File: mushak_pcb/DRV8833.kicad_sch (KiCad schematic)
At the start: 7 parts, among them M1 motor, M2 motor, U3 DRV8833PW

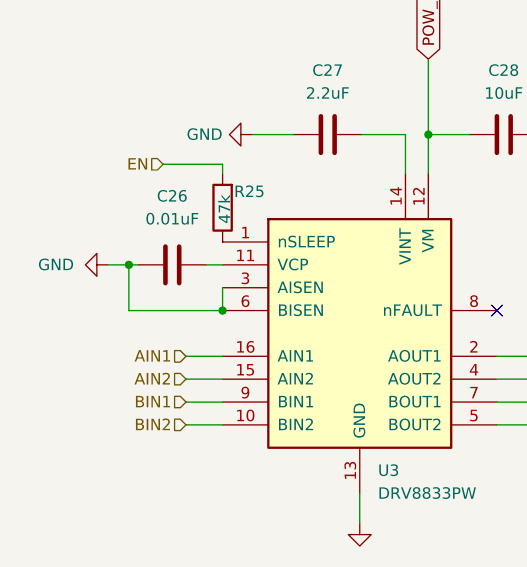
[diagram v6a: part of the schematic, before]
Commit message: corrected encoder and motor driver schematics
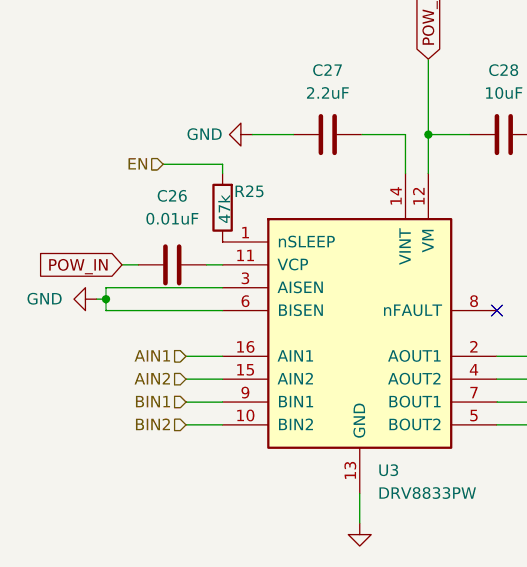
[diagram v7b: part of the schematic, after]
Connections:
- net GND: no longer C26.1
- net POW_IN: now also C26.1
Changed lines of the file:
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@@
     (comment 1 "Designed by - Chinmay Lonkar")
-  )
-  (junction (at 132.08 95.25) (diameter 0) (color 0 0 0 0)
   )
   (junction (at 154.94 75.692) (diameter 0) (color 0 0 0 0)
   )
-  (junction (at 121.666 90.17) (diameter 0) (color 0 0 0 0)
+  (junction (at 119.126 93.98) (diameter 0) (color 0 0 0 0)
   )
   (no_connect (at 162.56 95.25))
@@
     (stroke (width 0) (type default) (color 0 0 0 0))
   )
-  (wire (pts (xy 121.666 90.17) (xy 122.682 90.17))
-    (stroke (width 0) (type default) (color 0 0 0 0))
-  )
   (wire (pts (xy 162.56 107.95) (xy 202.438 107.95))
     (stroke (width 0) (type default) (color 0 0 0 0))
   )
-  (wire (pts (xy 119.38 90.17) (xy 121.666 90.17))
+  (wire (pts (xy 120.904 90.17) (xy 122.682 90.17))
     (stroke (width 0) (type default) (color 0 0 0 0))
   )
@@
     (stroke (width 0) (type default) (color 0 0 0 0))
   )
+  (wire (pts (xy 119.126 95.25) (xy 132.08 95.25))
+    (stroke (width 0) (type default) (color 0 0 0 0))
+  )
   (wire (pts (xy 154.94 75.692) (xy 159.512 75.692))
     (stroke (width 0) (type default) (color 0 0 0 0))
   )
   (wire (pts (xy 147.32 115.57) (xy 147.32 118.872))
+    (stroke (width 0) (type default) (color 0 0 0 0))
+  )
+  (wire (pts (xy 132.08 92.71) (xy 119.126 92.71))
     (stroke (width 0) (type default) (color 0 0 0 0))
   )
@@
     (stroke (width 0) (type default) (color 0 0 0 0))
   )
-  (wire (pts (xy 121.666 95.25) (xy 121.666 90.17))
-    (stroke (width 0) (type default) (color 0 0 0 0))
-  )
   (wire (pts (xy 128.016 100.33) (xy 132.08 100.33))
     (stroke (width 0) (type default) (color 0 0 0 0))
   )
   (wire (pts (xy 125.476 78.994) (xy 132.08 78.994))
+    (stroke (width 0) (type default) (color 0 0 0 0))
+  )
+  (wire (pts (xy 118.11 93.98) (xy 119.126 93.98))
     (stroke (width 0) (type default) (color 0 0 0 0))
   )
@@
     (stroke (width 0) (type default) (color 0 0 0 0))
   )
-  (wire (pts (xy 162.56 102.87) (xy 222.25 102.87))
+  (wire (pts (xy 119.126 93.98) (xy 119.126 95.25))
     (stroke (width 0) (type default) (color 0 0 0 0))
   )
-  (wire (pts (xy 132.08 92.71) (xy 132.08 95.25))
+  (wire (pts (xy 162.56 102.87) (xy 222.25 102.87))
     (stroke (width 0) (type default) (color 0 0 0 0))
   )
@@
     (stroke (width 0) (type default) (color 0 0 0 0))
   )
-  (wire (pts (xy 132.08 95.25) (xy 121.666 95.25))
+  (wire (pts (xy 119.126 92.71) (xy 119.126 93.98))
     (stroke (width 0) (type default) (color 0 0 0 0))
   )
   (wire (pts (xy 130.302 90.17) (xy 132.08 90.17))
     (stroke (width 0) (type default) (color 0 0 0 0))
+  )
+  (global_label "POW_IN" (shape input) (at 120.904 90.17 180) (fields_autoplaced)
+    (effects (font (size 1.27 1.27)) (justify right))
+    (property "Intersheet References" "${INTERSHEET_REFS}" (id 0) (at 111.5361 90.2494 0)
+      (effects (font (size 1.27 1.27)) (justify right) hide)
+    )
   )
   (global_label "POW_IN" (shape input) (at 154.94 67.31 90) (fields_autoplaced)
@@
     (pin "1")
   )
+  (symbol (lib_id "power:GND") (at 118.11 93.98 270) (unit 1)
+    (in_bom yes) (on_board yes) (fields_autoplaced)
+    (property "Reference" "#PWR0101" (id 0) (at 111.76 93.98 0)
+      (effects (font (size 1.27 1.27)) hide)
+    )
+    (property "Value" "GND" (id 1) (at 114.3 93.9799 90)
+      (effects (font (size 1.27 1.27)) (justify right))
+    )
+    (property "Footprint" "" (id 2) (at 118.11 93.98 0)
+      (effects (font (size 1.27 1.27)) hide)
+    )
+    (property "Datasheet" "" (id 3) (at 118.11 93.98 0)
+      (effects (font (size 1.27 1.27)) hide)
+    )
+    (pin "1")
+  )
   (symbol (lib_id "power:GND") (at 147.32 118.872 0) (unit 1)
     (in_bom yes) (on_board yes) (fields_autoplaced)
@@
       (effects (font (size 1.27 1.27)) hide)
     )
-    (pin "1")
-  )
-  (symbol (lib_id "power:GND") (at 119.38 90.17 270) (unit 1)
-    (in_bom yes) (on_board yes) (fields_autoplaced)
-    (property "Reference" "#PWR013" (id 0) (at 113.03 90.17 0)
-      (effects (font (size 1.27 1.27)) hide)
-    )
-    (property "Value" "GND" (id 1) (at 115.57 90.1699 90)
-      (effects (font (size 1.27 1.27)) (justify right))
-    )
-    (property "Footprint" "" (id 2) (at 119.38 90.17 0)
-      (effects (font (size 1.27 1.27)) hide)
-    )
-    (property "Datasheet" "" (id 3) (at 119.38 90.17 0)
-      (effects (font (size 1.27 1.27)) hide)
-    )
